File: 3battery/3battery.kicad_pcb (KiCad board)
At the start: 4 copper layers, 92.3 x 62.1 mm, 61 parts, among them J1 Barrel_Jack, J2 1 cell, J3 3 cells, J4 opt, J5 opt, J6 opt, Q1 BSL302SNH6327XTSA1, Q2 BSL302SNH6327XTSA1, Q3 CPH6350-TL-W, U1 bq24133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

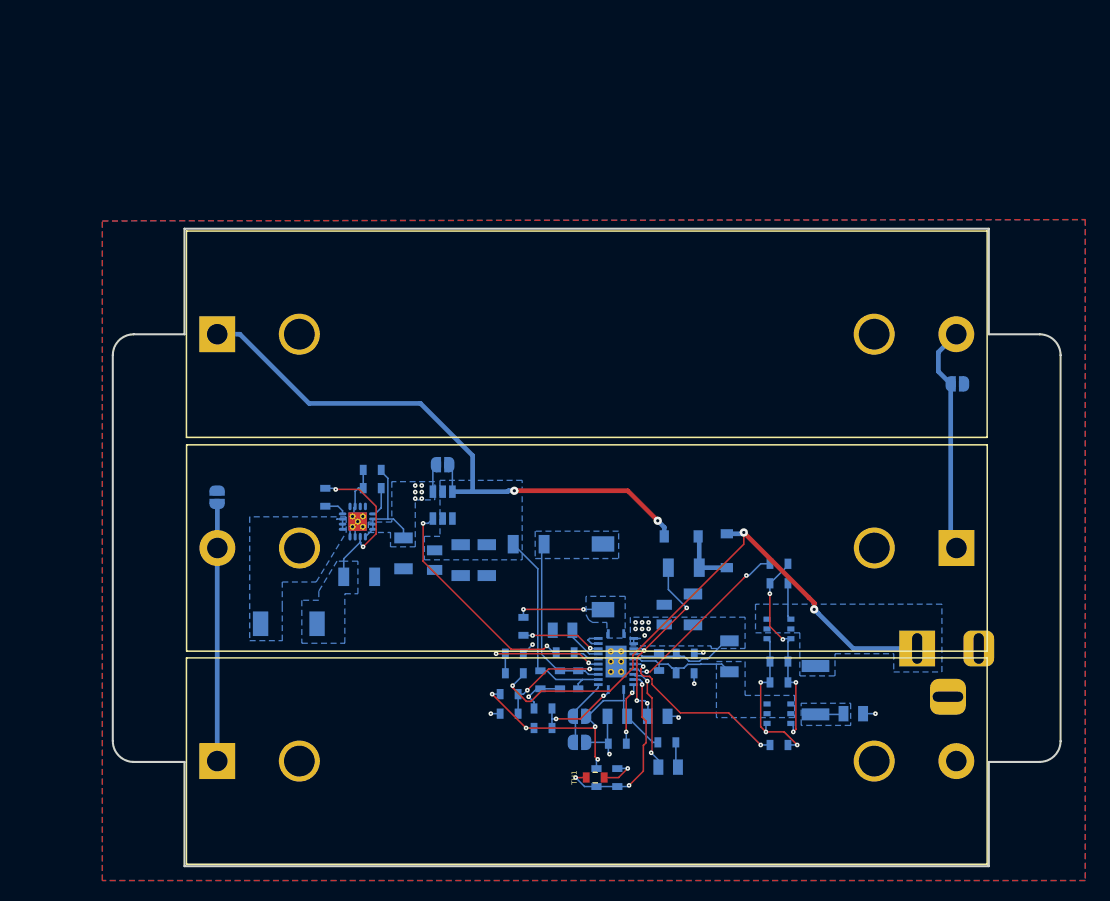
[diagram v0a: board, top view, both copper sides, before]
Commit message: Main board and proto-board added
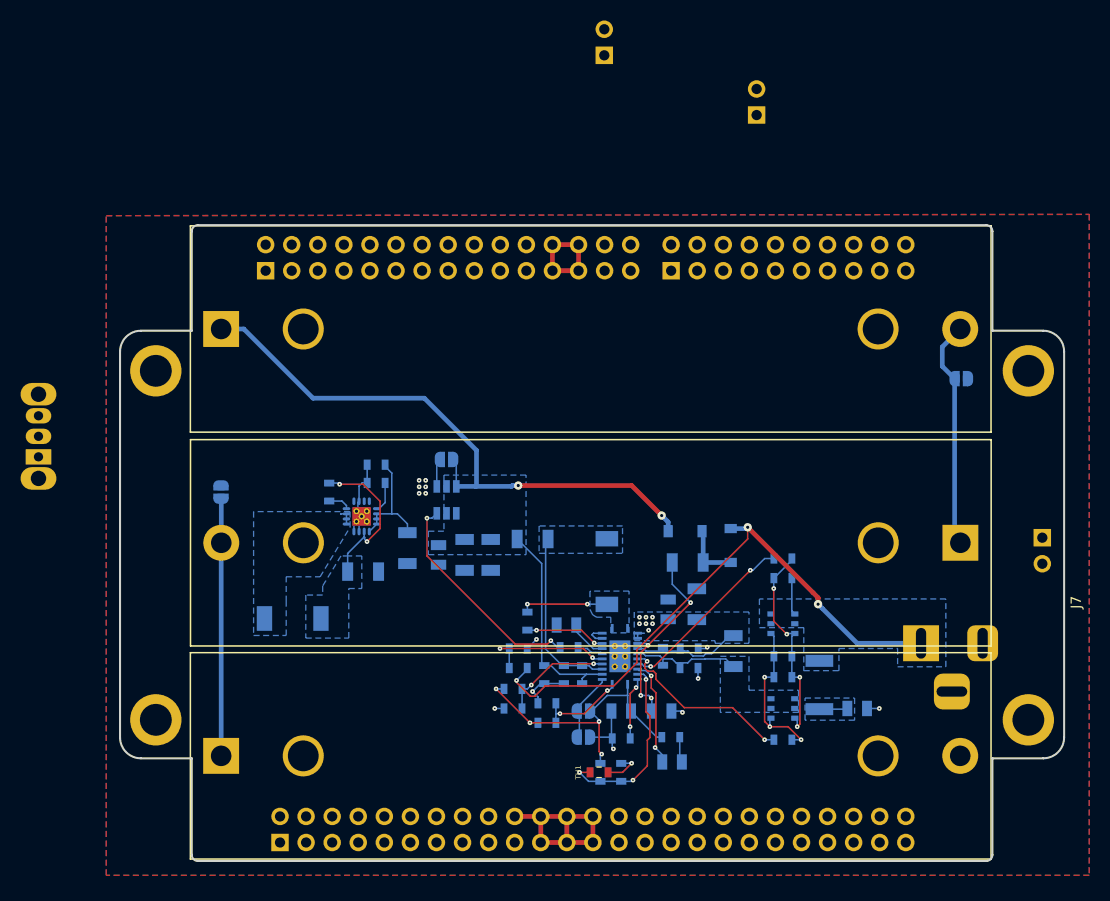
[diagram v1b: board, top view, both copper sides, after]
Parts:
- added J10: Conn_01x02, Connector_PinHeader_2.54mm:PinHeader_1x02_P2.54mm_Vertical, B.Cu at (159.1, 54.3)
- added J7: uniwersal-board2, iwasz:uniwersal-board, F.Cu at (143.1, 96.0)
- added J8: Conn_01x02, Connector_PinHeader_2.54mm:PinHeader_1x02_P2.54mm_Vertical, B.Cu at (186.9, 95.5)
- added J9: Conn_01x02, Connector_PinHeader_2.54mm:PinHeader_1x02_P2.54mm_Vertical, B.Cu at (144.3, 48.5)
- added SW1: SW_SPDT, Button_Switch_THT:SW_CuK_OS102011MA1QN1_SPDT_Angled, B.Cu at (89.2, 87.6)
- moved BT2 0.64 mm to (179.0, 96.0)
- moved C1 0.64 mm to (149.9, 112.4)
- moved C13 0.64 mm to (152.5, 108.2)
- moved C14 0.64 mm to (125.1, 96.5)
- moved C15 0.64 mm to (122.0, 88.4)
- moved C2 0.64 mm to (145.9, 112.4)
- moved C4 0.64 mm to (153.3, 102.0)
- moved J1 0.64 mm to (175.1, 105.8)
- moved J3 0.64 mm to (142.2, 112.4)
- moved Q1 0.64 mm to (161.7, 103.9)
- moved R12 0.64 mm to (161.7, 115.2)
- moved R14 0.64 mm to (140.8, 106.2)
- moved R2 0.64 mm to (138.7, 113.5)
- moved R3 0.64 mm to (138.7, 111.6)
- moved R6 0.64 mm to (135.9, 108.2)
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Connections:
- BT3 pad 2: GNDD -> GND
- C10 pad 1: GNDD -> GND
- C14 pad 1: GNDD -> GND
- C14 pad 2: +BATT -> +12V
- C15 pad 1: +BATT -> +12V
- C15 pad 2: GNDD -> GND
- C16 pad 1: GNDD -> GND
- C17 pad 2: GNDD -> GND
- C21 pad 1: GNDD -> GND
- C22 pad 1: GNDD -> GND
- C4 pad 1: GNDD -> GND
- C6 pad 1: GNDD -> GND
- C9 pad 1: GNDD -> GND
- J1 pad 2: GNDD -> GND
- J4 pad 2: GNDD -> GND
- J5 pad 2: GNDD -> GND
- U1 pad 22: GNDD -> GND
- U1 pad 23: GNDD -> GND
- U2 pad 10: +BATT -> +12V
- U2 pad 11: +BATT -> +12V
- U2 pad 12: +BATT -> +12V
- U2 pad 13: +BATT -> +12V
- U2 pad 15: GNDD -> GND
- U2 pad 16: GNDD -> GND
- U2 pad 17: GNDD -> GND
- U2 pad 5: GNDD -> GND
- U2 pad 6: GNDD -> GND
- U2 pad 7: GNDD -> GND
- U2 pad 8: GNDD -> GND
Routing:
- net +12V: track 0.00 -> 31.7 mm
- net +BATT: track 26.8 -> 15.5 mm
- net +5V: track 15.3 -> 25.4 mm
- net GND: track 21.2 -> 31.3 mm
- net GNDD: track 9.63 -> 0.00 mm
- added copper zone on B.Cu, net GND
- added copper zone on In1.Cu, net GND
- added copper zone on In2.Cu, net GND
- removed copper zone on B.Cu, net GNDD
- removed copper zone on In1.Cu, net GNDD
- removed copper zone on In2.Cu, net GNDD
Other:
- board size 92.3 x 62.1 mm -> 92 x 61.9 mm
- board text added: "Franek & tata iwasz.pl 3 cell charger V1"
- board text removed: "Franek & tata 3 cell charger V1"
- board text removed: "Połączyć GND i GNDD pod thermal padami IC Doczytać application notes Poroboć VIA stiching"

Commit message: 4 layers, but I plan to make it only 2.
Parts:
- moved J9 71.4 mm to (138.2, 119.6), turned to 90 degrees
- moved L2 45.2 mm to (148.8, 74.7), turned to 0 degrees
- moved J10 29.0 mm to (136.7, 72.6), turned to 270 degrees
- moved C17 28.8 mm to (142.0, 79.2), turned to 180 degrees
- moved R13 28.1 mm to (145.3, 87.0), turned to 270 degrees
- moved U2 23.2 mm to (142.1, 84.6), turned to 180 degrees
- moved C14 19.5 mm to (137.6, 81.5), turned to 270 degrees
- moved C16 18.8 mm to (140.7, 87.9), turned to 180 degrees
- moved C15 18.7 mm to (140.7, 89.7), turned to 0 degrees
- moved SW1 10.7 mm to (99.6, 89.9)
- moved Q3 5.87 mm to (134.4, 89.7), turned to 0 degrees
- moved J6 5.61 mm to (134.4, 86.6), turned to 180 degrees
- moved J8 2.17 mm to (184.9, 94.7), turned to 270 degrees
- moved J1 2.16 mm to (175.3, 103.6)
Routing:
- net +12V: track 31.7 -> 114.7 mm, vias 0 -> 1
- net +BATT: track 15.5 -> 55.0 mm, vias 13 -> 12
- net /SRN: track 79.8 -> 74.7 mm
- net +15V: track 60.4 -> 63.6 mm
- net Net-(Q3-Pad2): track 21.8 -> 24.9 mm
- net Net-(C5-Pad2): track 7.83 -> 9.57 mm
- net Net-(L2-Pad2): track 1.59 -> 2.68 mm
- net GND: track 31.3 -> 30.3 mm
- net Net-(C5-Pad1): track 8.53 -> 9.29 mm
- net /SRP: track 17.1 -> 17.9 mm
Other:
- board text added: "12V"
- board text added: "5V"
- board text added: "in 13V-17V"

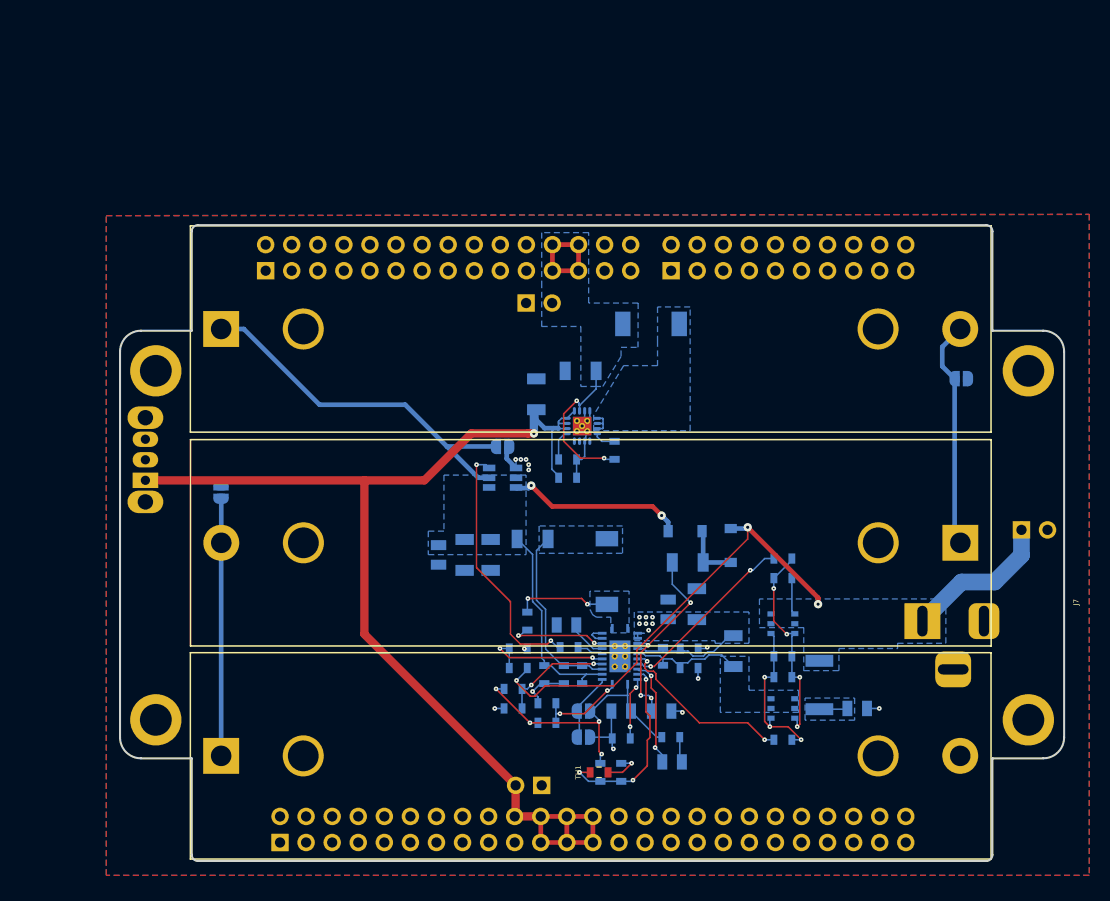
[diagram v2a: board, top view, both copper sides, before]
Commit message: Gerbers directory added, and domcumentation improved
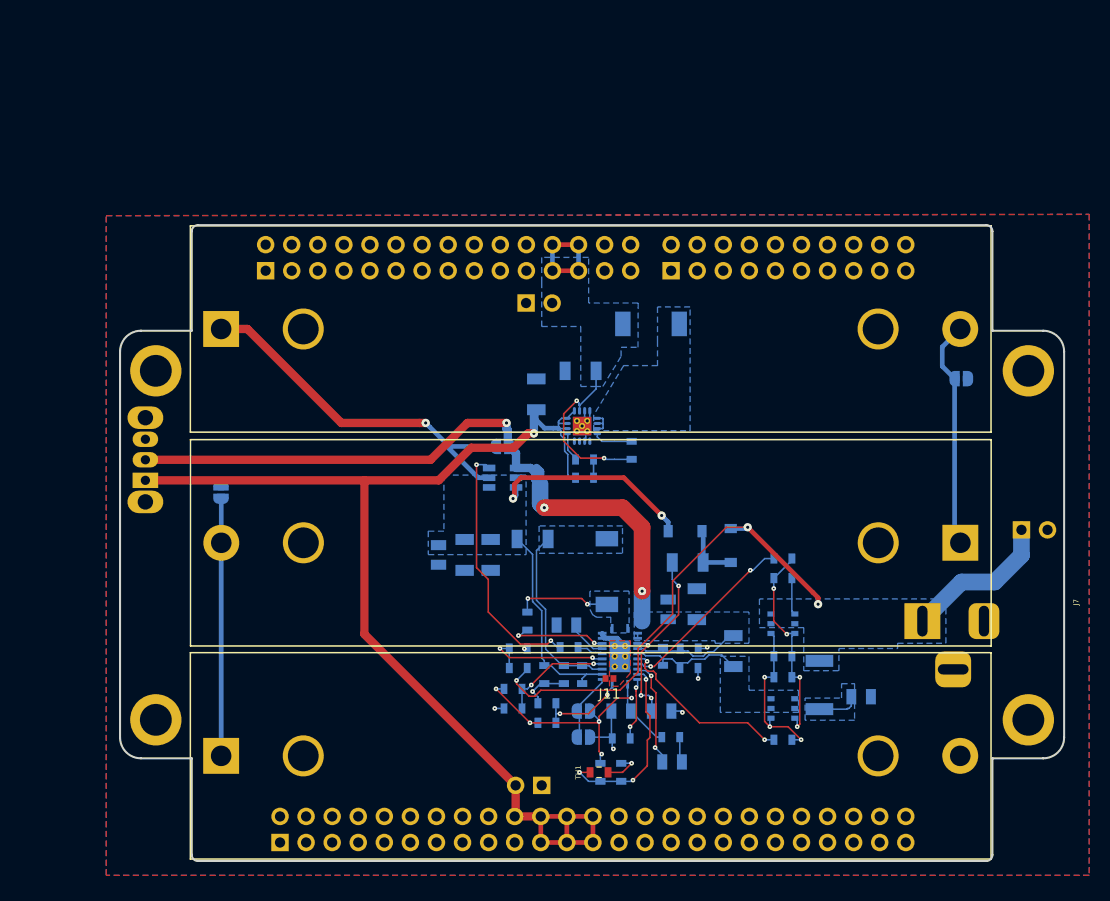
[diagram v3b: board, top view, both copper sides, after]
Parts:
- added J11: opt, Resistor_SMD:R_0402_1005Metric, F.Cu at (144.8, 109.2)
- moved R13 1.67 mm to (146.9, 87.0)
- moved C15 1.65 mm to (142.3, 89.7)
- moved C16 1.65 mm to (142.3, 87.9)
- moved Cin1 1.20 mm to (169.3, 111.0)
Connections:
- BT3 pad 2: GND -> GNDD
- C10 pad 1: GND -> GNDD
- C14 pad 1: GND -> GNDD
- C15 pad 2: GND -> GNDD
- C16 pad 1: GND -> GNDD
- C17 pad 2: GND -> GNDD
- C21 pad 1: GND -> GNDD
- C22 pad 1: GND -> GNDD
- C4 pad 1: GND -> GNDD
- C6 pad 1: GND -> GNDD
- C9 pad 1: GND -> GNDD
- Cin1 pad 2: GND -> GNDD
- J1 pad 2: GND -> GNDD
- J10 pad 1: GND -> GNDD
- J4 pad 2: GND -> GNDD
- J5 pad 2: GND -> GNDD
- J8 pad 2: GND -> GNDD
- J9 pad 1: GND -> GNDD
- U1 pad 22: GND -> GNDD
- U1 pad 23: GND -> GNDD
- U1 pad 25: GND -> GNDD
- U2 pad 15: GND -> GNDD
- U2 pad 16: GND -> GNDD
- U2 pad 17: GND -> GNDD
- U2 pad 5: GND -> GNDD
- U2 pad 6: GND -> GNDD
- U2 pad 7: GND -> GNDD
- U2 pad 8: GND -> GNDD
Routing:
- net +BATT: track 55.0 -> 82.3 mm, vias 12 -> 3
- net GNDD: track 0.00 -> 11.3 mm
- net GND: track 30.3 -> 19.0 mm, vias 9 -> 8
- net /SRN: track 74.7 -> 78.1 mm, vias 2 -> 3
- net +15V: track 63.6 -> 65.5 mm
- net Net-(R13-Pad1): track 2.17 -> 3.84 mm
- net +5V: track 25.4 -> 27.1 mm
- net Net-(Cin1-Pad1): track 2.76 -> 4.14 mm
- net Net-(C1-Pad1): track 19.2 -> 18.2 mm
- net /VREF: track 30.0 -> 30.9 mm, vias 4 -> 5
- net +12V: track 114.7 -> 115.3 mm
- added copper zone on B.Cu, net GNDD
- added copper zone on F.Cu, net GNDD
- removed copper zone on In1.Cu, net +BATT
- removed copper zone on B.Cu, net GND
- removed copper zone on In1.Cu, net GND
- removed copper zone on In2.Cu, net GND
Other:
- copper layers 4 -> 2

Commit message: Bug-fixes. 3 battery soldered and working.
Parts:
- added D4: LED, Diode_SMD:D_0805_2012Metric, B.Cu at (106.7, 67.4)
- added R16: 680R, Resistor_SMD:R_0603_1608Metric, B.Cu at (106.8, 70.2)
- J3: footprint Jumper:SolderJumper-2_P1.3mm_Open_RoundedPad1.0x1.5mm -> Jumper:SolderJumper-2_P1.3mm_Bridged_RoundedPad1.0x1.5mm
- R10: value 680R -> 560
- moved D3 28.5 mm to (178.6, 124.1)
- moved R10 28.5 mm to (178.4, 121.7)
- moved TH1 15.3 mm to (130.7, 110.4)
- moved J1 1.27 mm to (175.3, 104.9)
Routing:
- net /VREF: track 30.9 -> 64.2 mm, vias 5 -> 7
- net +5V: track 27.1 -> 60.2 mm
- net Net-(D3-Pad1): track 10.5 -> 37.5 mm
- net Net-(R8-Pad1): track 18.5 -> 33.3 mm
- net Net-(D4-Pad2): track 0.00 -> 3.65 mm
- net GND: track 19.0 -> 16.4 mm
- net +15V: track 65.5 -> 67.4 mm
- net +BATT: track 82.3 -> 84.0 mm
- net Net-(L2-Pad2): track 2.68 -> 3.78 mm
- net /SRN: track 78.1 -> 77.0 mm
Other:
- board text added: "+"
- board text added: "-"
- board text added: "3 cells 1 cell"
- board text added: "5V on"
- board text added: "Franek & tata iwasz.pl 3 cell charger 1.1"
- board text added: "ON"
- board text added: "Warning. Trim barell jack socket terminals before soldering."
- board text added: "charging"
- board text added: "in 13V-17V 2A+"
- board text removed: "Franek & tata iwasz.pl 3 cell charger V1"
- board text removed: "in 13V-17V"
